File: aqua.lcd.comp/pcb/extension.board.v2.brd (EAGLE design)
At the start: 100.3 x 63.2 mm, 52 parts, among them IC1 NCP1117ST50T3G, K2 JS-M1-9V-4, Q1 BC447, T1 IRFR024NPBF, T10 BC847BSMD, T11 IRFR024NPBF, T12 BC847BSMD, T2 BC847BSMD, T3 IRFR024NPBF, T4 BC847BSMD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

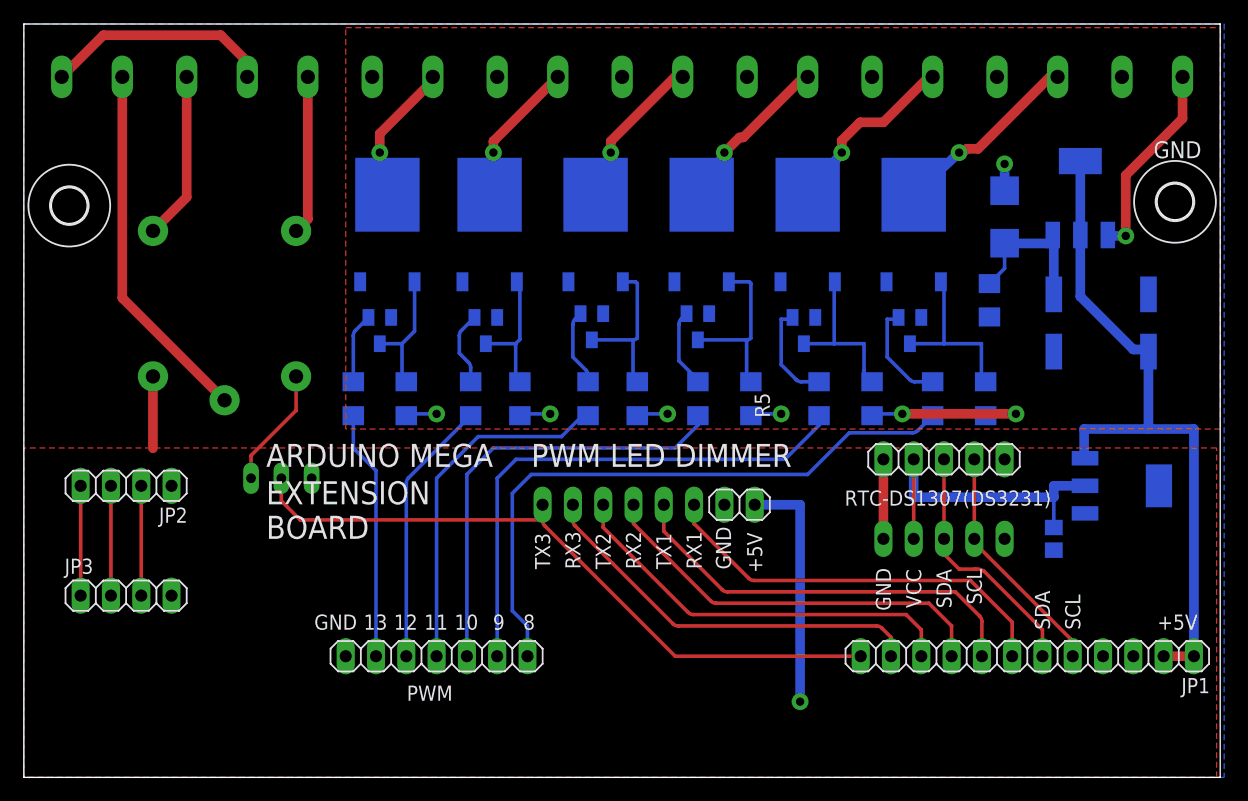
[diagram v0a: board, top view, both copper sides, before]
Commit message: extension board modified
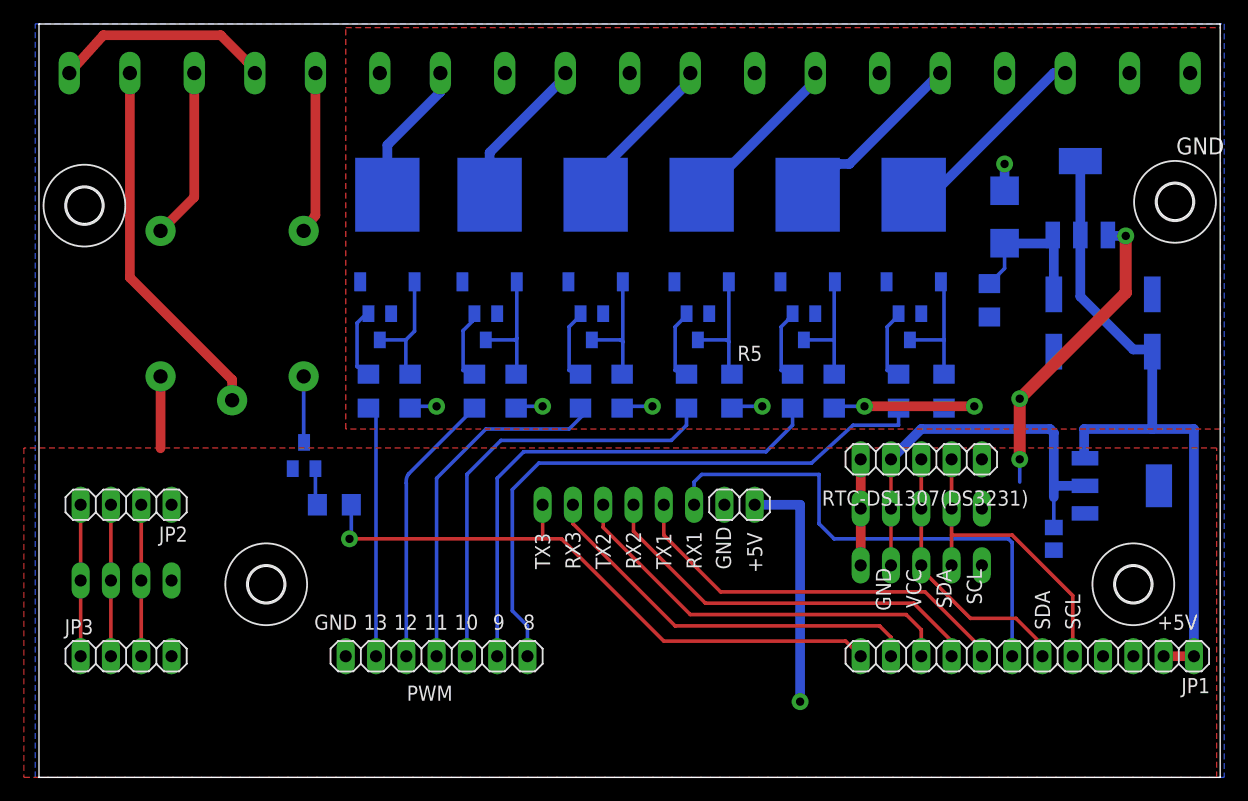
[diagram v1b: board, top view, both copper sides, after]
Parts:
- removed Q1: BC447, transistor-npn:TO92-EBC
- removed X1: (no value), con-wago-508:W237-132
- removed X3: (no value), con-wago-508:W237-3E
- added 230V: (no value), con-wago-508:W237-132
- added JP4: (no value), pinhead:1X04
- added OUT230V: (no value), con-wago-508:W237-3E
- added R12: 680, rcl:R1206
- added RTC-DS1307(DS3231)2: (no value), pinhead:1X05
- added T13: BC847BSMD, transistor-npn:SOT23
- added U$3, U$4: (no value), holes:3,0
- moved JP3 5.08 mm to (-11.7, 3.17)
- moved R10 3.55 mm to (56.8, 25.4)
- moved R8 3.24 mm to (47.6, 25.4)
- moved R11 2.93 mm to (53.0, 25.4)
- moved RTC-DS1307(DS3231)1 2.93 mm to (54.9, 10.8)
- moved R9 2.31 mm to (44.1, 25.4)
- moved RTC-DS1307(DS3231) 1.91 mm to (54.9, 19.7)
- moved R5 1.71 mm to (39.1, 25.4)
- moved JP2 1.59 mm to (-11.7, 15.9)
- moved R16 1.42 mm to (8.57, 25.4)
- moved R3 1.42 mm to (29.8, 25.4)
- moved U$2 1.27 mm to (-15.2, 41.0)
- moved R7 1.14 mm to (35.2, 25.4)
- moved R4 0.90 mm to (26.4, 25.4)
- moved 7.0-30V 0.71 mm to (74.9, 51.4)
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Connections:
- new net N$34: R12.2, T13.1
- net +5V: now also JP4.1
- net 3.3V: now also RTC-DS1307(DS3231)2.2
- net GND: now also JP4.3, RTC-DS1307(DS3231)2.1, T13.2; no longer Q1.E
- net N$1: now also 230V.1, OUT230V.2; no longer X1.1, X3.2
- net N$14: now also OUT230V.1; no longer X3.1
- net N$2: now also 230V.2; no longer X1.2
- net N$26: now also JP4.4
- net N$37: now also OUT230V.3; no longer X3.3
- net N$41: now also T13.3; no longer Q1.C
- net OUT: now also JP4.2
- net SCL: now also RTC-DS1307(DS3231)2.4
- net SDA: now also RTC-DS1307(DS3231)2.3
- net TX3: now also R12.1; no longer Q1.B
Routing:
- net GND: track 32.7 -> 52.6 mm, vias 1 -> 3
- net N$3: track 34.5 -> 43.1 mm
- net 3.3V: track 27.7 -> 34.3 mm
- net SCL: track 19.8 -> 26.2 mm
- net TX3: track 57.3 -> 52.7 mm, vias 0 -> 1
- net N$41: track 10.1 -> 5.55 mm
- net N$32: track 14.6 -> 10.7 mm
- net N$26: track 9.21 -> 12.7 mm
- net OUT: track 9.21 -> 12.7 mm
- net N$29: track 13.7 -> 10.3 mm
- net N$22: track 14.6 -> 11.3 mm
- net N$34: track 0.00 -> 3.10 mm
- net N$31: track 8.79 -> 6.16 mm
- net N$28: track 8.52 -> 6.13 mm
- net N$19: track 13.3 -> 11.2 mm
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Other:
- board size 100.3 x 63.2 mm -> 99 x 63.2 mm
- board text added: "ARDUINO MEGA AQUARIUM EXTENSION BOARD"
- board text removed: "ARDUINO MEGA"
- board text removed: "EXTENSION BOARD"
- board text removed: "PWM LED DIMMER"

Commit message: add temperature reading
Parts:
- added R13, R14: 4k7, rcl:R1206
- R1, R10, R3, R5, R6, R8: value 1K -> 2k2
- R11, R12, R16, R2, R4, R7, R9: value 680 -> 4k7
- moved JP4 2.48 mm to (-10.2, 11.4)
- moved JP2 2.25 mm to (-10.2, 17.5)
- moved JP3 1.59 mm to (-10.2, 3.17)
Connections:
- removed net N$26: JP2.4, JP3.1, JP4.4
- removed net OUT: JP2.2, JP3.3, JP4.2
- new net A0: JP2.2, JP3.3, JP4.2, R13.2
- new net A1: JP2.3, JP3.2, JP4.3, R14.2
- net GND: now also JP2.4, JP3.1, JP4.4, R13.1, R14.1; no longer JP2.3, JP3.2, JP4.3
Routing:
- net A0: track 0.00 -> 19.7 mm
- net A1: track 0.00 -> 18.5 mm
- net N$26: track 12.7 -> 0.00 mm
- net OUT: track 12.7 -> 0.00 mm
- net GND: track 52.6 -> 62.2 mm

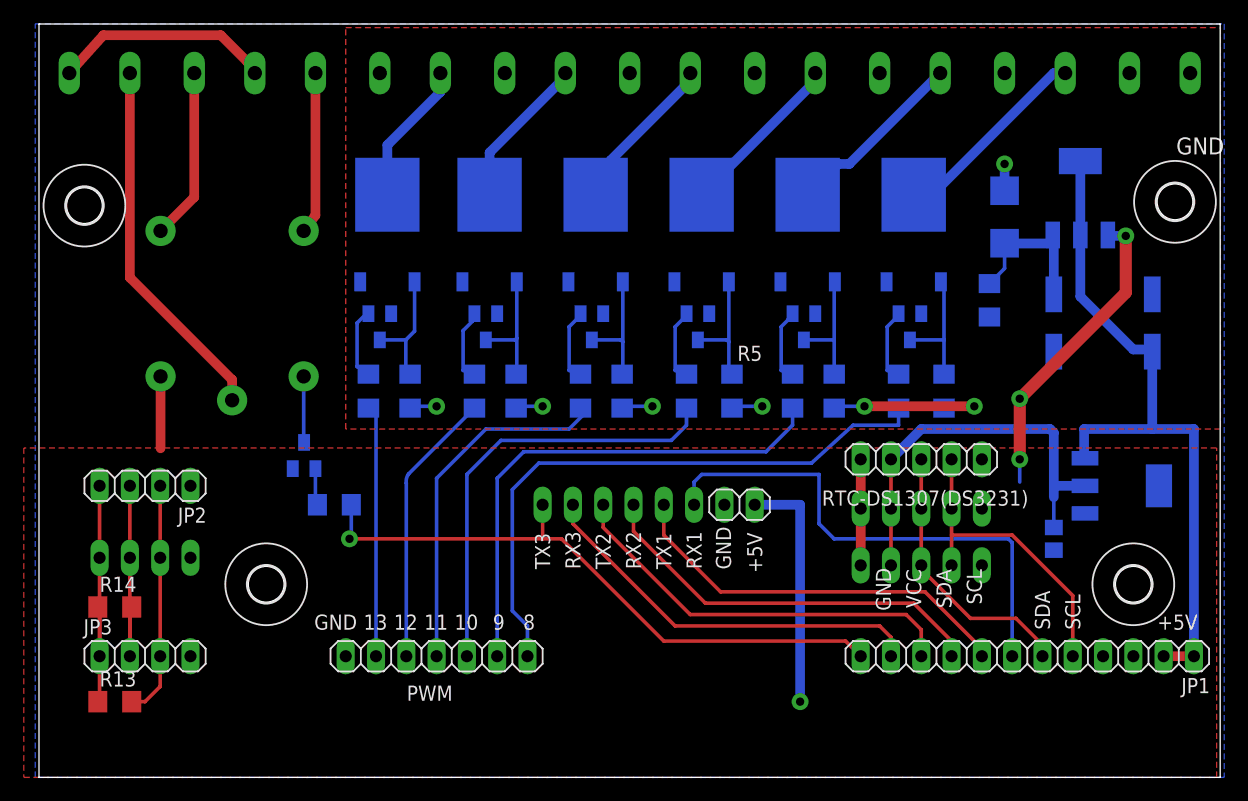
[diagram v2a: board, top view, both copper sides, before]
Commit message: add thermistor
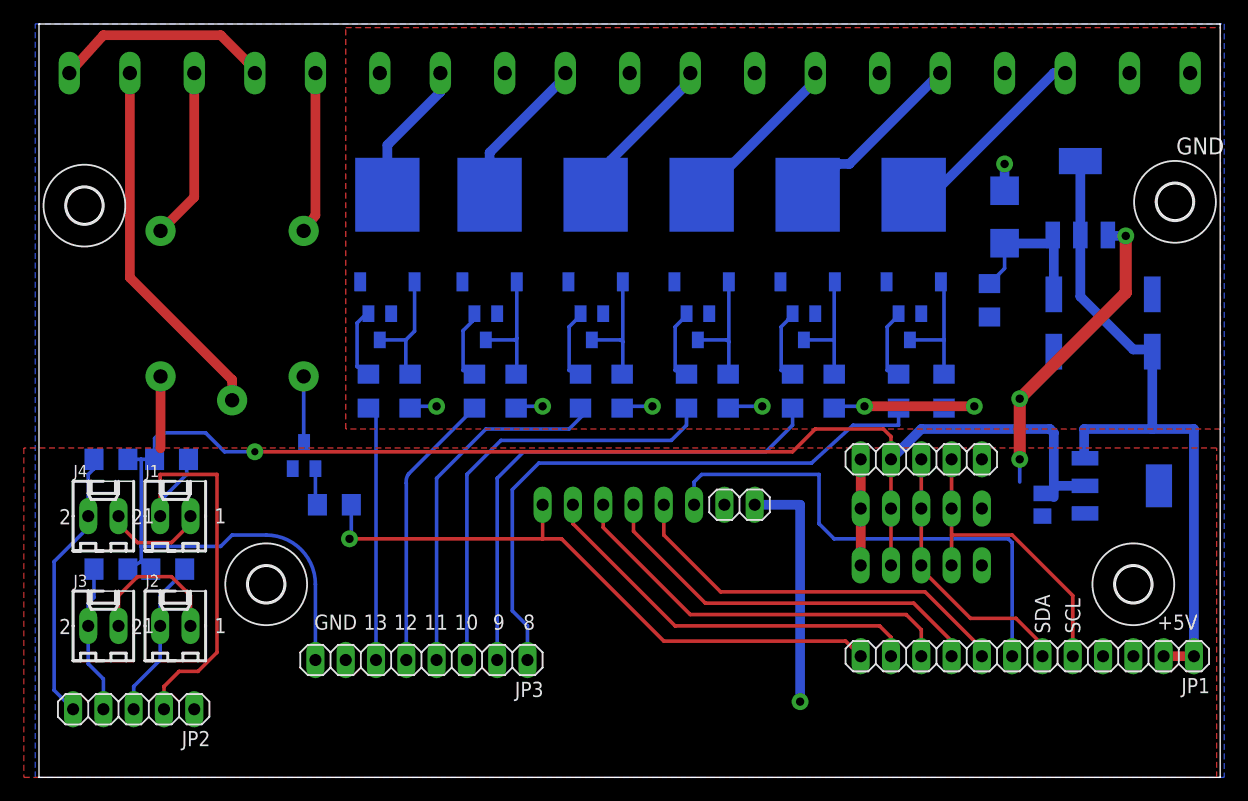
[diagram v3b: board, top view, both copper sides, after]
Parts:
- removed JP4: (no value), pinhead:1X04
- removed PC1: 47u, rcl:PANASONIC_D
- removed PWM: (no value), pinhead:1X07
- added C4: 1u, rcl:C0805
- added J1, J2, J3, J4: 22-27-2021-02, con-molex:6410-02
- added R15, R17: 4k7, rcl:R1206
- C1: value (none) -> 47u; device rcl:C0805 -> rcl:PANASONIC_D
- C2: value (none) -> 100n
- JP2: device pinhead:1X04 -> pinhead:1X05
- JP3: device pinhead:1X04 -> pinhead:1X08
- R10, R8: value 2k2 -> 4k7
- R2, R4: value 4k7 -> 2k2
- moved R12 48.3 mm to (53.0, 25.4), turned to 270 degrees
- moved R6 44.8 mm to (56.8, 25.4)
- moved R8 30.2 mm to (17.5, 25.4), turned to 270 degrees
- moved R7 26.7 mm to (8.57, 25.4)
- moved R16 26.2 mm to (-13.0, 10.5), turned to 180 degrees
- moved R13 24.7 mm to (5.71, 15.9), flipped to the bottom
- moved JP3 23.2 mm to (13.0, 2.86), turned to 180 degrees
- moved R10 21.6 mm to (35.2, 25.4), turned to 270 degrees
- moved JP2 18.8 mm to (-11.1, -1.27)
- moved C1 18.1 mm to (66.0, 31.1), turned to 90 degrees
- moved R9 17.8 mm to (26.4, 25.4)
- moved R14 13.3 mm to (-7.94, 19.7), flipped to the bottom
- moved R4 12.4 mm to (38.7, 25.4), turned to 90 degrees
- moved R11 8.89 mm to (44.1, 25.4)
- moved R1 8.89 mm to (12.1, 25.4)
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- renumbered 7.0-30V to 12VIN, K2 to RELE, PC2 to C3, RTC-DS1307(DS3231)1 to +, RTC-DS1307(DS3231)2 to _
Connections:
- removed net A0: JP2.2, JP3.3, JP4.2, R13.2
- removed net A1: JP2.3, JP3.2, JP4.3, R14.2
- new net N$26: J4.2, JP2.5, R17.1
- new net N$39: J3.2, JP2.4, R16.1
- new net N$43: J1.2, JP2.2, R14.1
- new net N$45: J2.2, JP2.3, R15.1
- new net VCC: R4.1
- net +5V: no longer JP2.1, JP3.4, JP4.1
- net 3.3V: now also C4.1, JP3.8, R14.2, R15.2, R16.2, R17.2; no longer C1.1
- net GND: now also C1.-, C4.2, J1.1, J2.1, J3.1, J4.1, JP3.7; no longer C1.2, JP2.4, JP3.1, JP4.4, PC1.-, PWM.7, R13.1, R14.1
- net N$10: now also JP3.6, R7.2; no longer PWM.6, R16.2
- net N$11: now also R7.1; no longer R16.1
- net N$12: now also R1.2; no longer R6.2
- net N$15: now also R8.1; no longer R2.1
- net N$16: now also R2.2; no longer R1.2
- net N$18: now also R9.1; no longer R4.1
- net N$21: now also R10.1; no longer R7.1
- net N$22: now also R4.2; no longer R5.2
- net N$28: now also R11.1; no longer R9.1
- net N$29: now also R5.2; no longer R8.2
- net N$31: now also R12.1; no longer R11.1
- net N$32: now also R6.2; no longer R10.2
- net N$34: now also R13.2; no longer R12.2
- net N$5: now also JP3.1, R12.2; no longer PWM.1, R11.2
- net N$6: now also JP3.2, R11.2; no longer PWM.2, R9.2
- net N$7: now also JP3.3, R10.2; no longer PWM.3, R7.2
- net N$8: now also JP3.4, R9.2; no longer PWM.4, R4.2
- net N$9: now also JP3.5, R8.2; no longer PWM.5, R2.2
- net PWRIN: now also R2.1; no longer R10.1, R8.1
- net TX3: now also R13.1; no longer R12.1
- net VIN: now also C1.+; no longer PC1.+
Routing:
- net 3.3V: track 34.3 -> 136.2 mm, vias 0 -> 1
- net N$43: track 0.00 -> 36.5 mm
- net N$26: track 0.00 -> 23.0 mm
- net A0: track 19.7 -> 0.00 mm
- net A1: track 18.5 -> 0.00 mm
- net N$45: track 0.00 -> 13.5 mm
- net N$39: track 0.00 -> 12.5 mm
- net GND: track 62.2 -> 60.9 mm
- net N$22: track 11.3 -> 10.5 mm
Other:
- board text added: "3.3V"
- board text removed: "VCC"

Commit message: fix button local colors
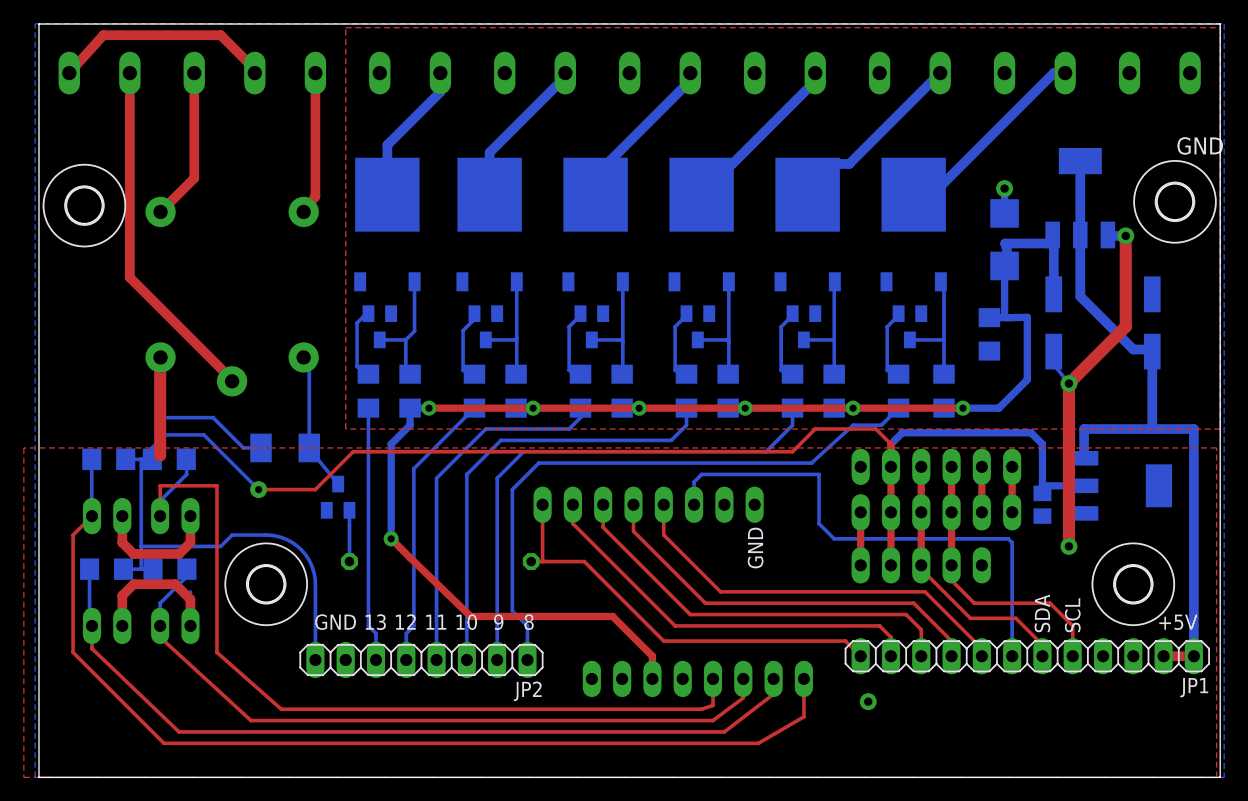
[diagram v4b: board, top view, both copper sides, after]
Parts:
- removed +, RTC-DS1307(DS3231), _: (no value), pinhead:1X05
- removed J3, J4: 22-27-2021-02, con-molex:6410-02
- added D2: (no value), diode:DO-214AC
- added JP4, JP5: (no value), pinhead:1X06
- added JP6: (no value), pinhead:1X08
- added TE3, TE4: 22-27-2021-02, con-molex:6410-02
- JP2: device pinhead:1X05 -> pinhead:1X08
- JP3: device pinhead:1X08 -> pinhead:1X05
- R13: value 4k7 -> (none); device rcl:R1206 -> rcl:0207/15
- moved JP3 42.7 mm to (54.9, 10.8), flipped to the bottom
- moved JP2 24.5 mm to (13.0, 2.86)
- moved R13 10.1 mm to (14.6, 11.1)
- moved T13 4.51 mm to (6.03, 16.5)
- moved C2 2.86 mm to (60.6, 30.2)
- moved D1 1.91 mm to (61.9, 38.1)
- moved RELE 1.59 mm to (-2.86, 34.9)
- moved R16 0.37 mm to (-13.4, 10.5)
- moved R14 0.18 mm to (-8.12, 19.7)
- moved R15 0.18 mm to (-8.07, 10.5)
- moved R17 0.18 mm to (-13.2, 19.7)
- flipped GND to the bottom
- flipped TE1 to the bottom, turned to 180 degrees
- flipped TE2 to the bottom, turned to 180 degrees
- renumbered J1 to TE1, J2 to TE2
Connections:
- removed net VCC: R4.1
- new net N$46: JP4.5, JP5.5
- new net N$47: JP4.6, JP5.6
- net +5V: now also D2.C
- net 3.3V: now also JP2.8, JP3.2, JP4.2, JP5.2; no longer +.2, JP3.8, RTC-DS1307(DS3231).2, _.2
- net GND: now also JP2.7, JP3.1, JP4.1, JP5.1, JP6.1, JP6.2, TE3.1, TE4.1; no longer +.1, J3.1, J4.1, JP3.7, RTC-DS1307(DS3231).1, _.1
- net N$10: now also JP2.6; no longer JP3.6
- net N$26: now also JP6.8, TE3.2; no longer J4.2, JP2.5
- net N$39: now also JP6.7, TE4.2; no longer J3.2, JP2.4
- net N$41: now also D2.A
- net N$43: now also JP6.5; no longer JP2.2
- net N$45: now also JP6.6; no longer JP2.3
- net N$5: now also JP2.1; no longer JP3.1
- net N$6: now also JP2.2; no longer JP3.2
- net N$7: now also JP2.3; no longer JP3.3
- net N$8: now also JP2.4; no longer JP3.4
- net N$9: now also JP2.5; no longer JP3.5
- net PWRIN: no longer R1.1, R2.1, R3.1, R5.1, R6.1
- net SCL: now also JP3.4, JP4.4, JP5.4; no longer +.4, RTC-DS1307(DS3231).4, _.4
- net SDA: now also JP3.3, JP4.3, JP5.3; no longer +.3, RTC-DS1307(DS3231).3, _.3
- net VIN: now also JP6.3, R1.1, R2.1, R3.1, R4.1, R5.1, R6.1
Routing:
- net VIN: track 13.0 -> 123.5 mm, vias 0 -> 7
- net N$26: track 23.0 -> 85.1 mm
- net N$39: track 12.5 -> 69.1 mm
- net N$45: track 13.5 -> 60.5 mm
- net N$43: track 36.5 -> 72.6 mm
- net PWRIN: track 27.0 -> 2.09 mm, vias 7 -> 1
- net TX3: track 52.7 -> 35.7 mm, vias 1 -> 0
- net N$41: track 5.55 -> 13.0 mm
- net N$47: track 0.00 -> 3.81 mm
- net N$46: track 0.00 -> 3.81 mm
- net +5V: track 85.4 -> 82.1 mm
- net SCL: track 26.2 -> 23.8 mm
- net 3.3V: track 136.2 -> 138.3 mm
- net N$2: track 31.0 -> 29.4 mm
- net N$37: track 13.6 -> 12.0 mm
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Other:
- board text added: "A0"
- board text added: "A1"
- board text added: "A2"
- board text added: "A3"
- board text added: "NC"
- board text added: "VIN"

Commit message: modified for makefile https://github.com/sudar/Arduino-Makefile
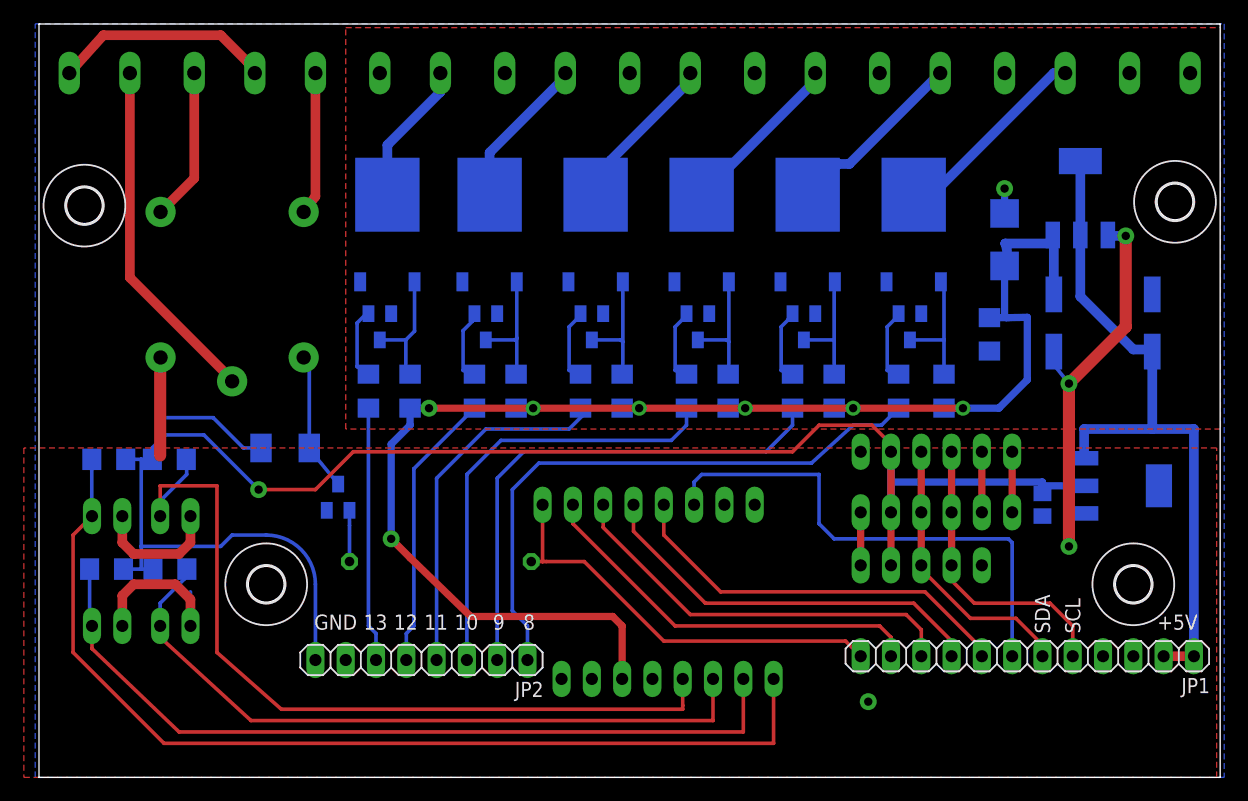
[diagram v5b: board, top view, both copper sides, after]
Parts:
- moved JP6 2.54 mm to (33.7, 1.27)
- moved JP5 1.27 mm to (56.2, 20.3)
- renumbered LED10 to RED, LED11 to COOLW, LED12 to WARMW, LED13 to CH13, LED8 to BLUE, LED9 to GREEN
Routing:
- net N$43: track 72.6 -> 70.4 mm
- net SCL: track 23.8 -> 25.1 mm
- net SDA: track 22.3 -> 23.6 mm
- net N$47: track 3.81 -> 5.08 mm
- net N$46: track 3.81 -> 5.08 mm
- net N$45: track 60.5 -> 59.2 mm
- net VIN: track 123.5 -> 122.4 mm
- net N$26: track 85.1 -> 84.1 mm
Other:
- board text added: "+V"
- board text added: "THERMISTORS"
